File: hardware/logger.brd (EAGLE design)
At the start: 33.5 x 32.9 mm, 40 parts, among them J1 MICRO_USB_B_HIROSE_ZX62-B-5PA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, SW1 TVAF06-A020B-R, U2 NJM12888F, X1 FA-238

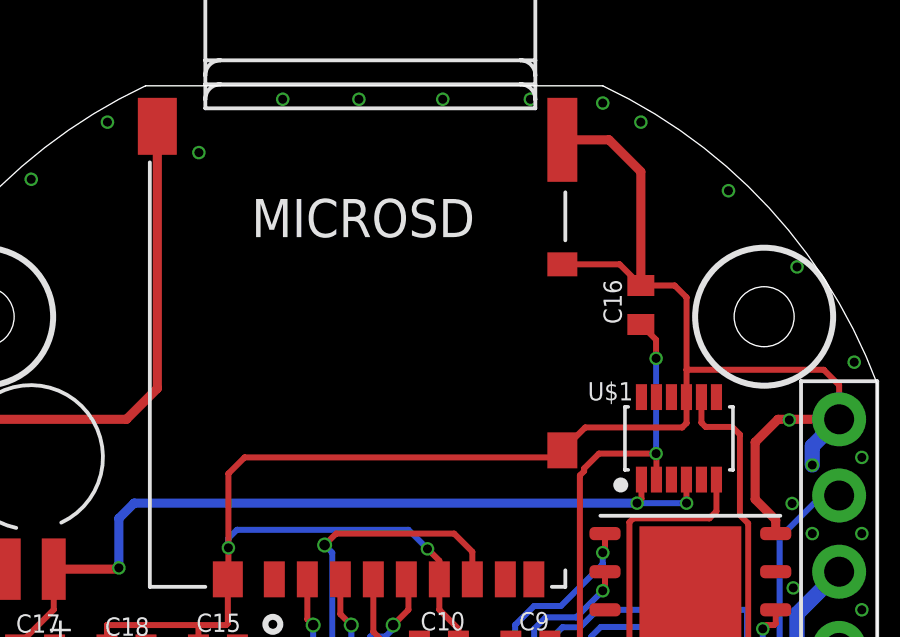
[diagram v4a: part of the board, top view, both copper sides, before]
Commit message: シルクを調整
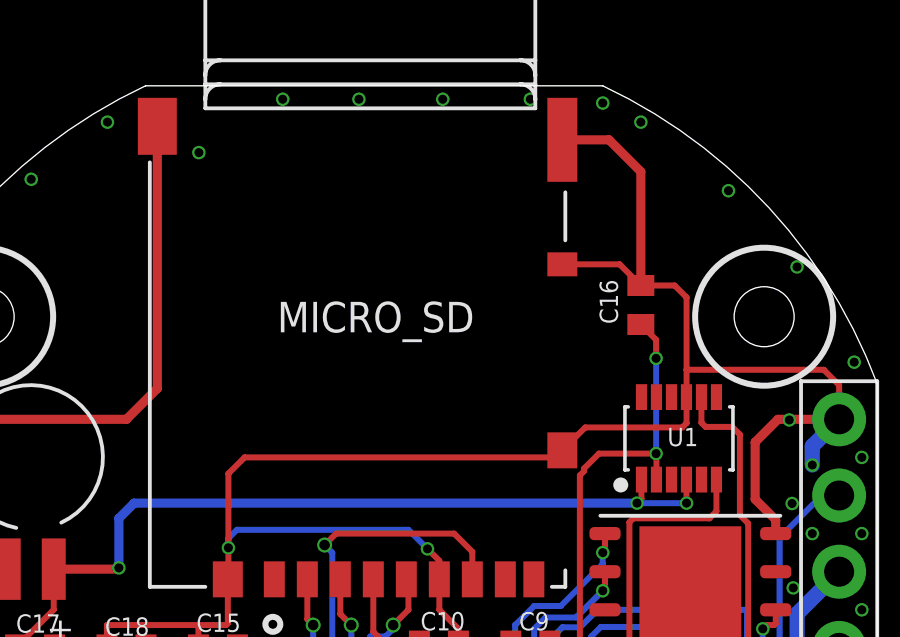
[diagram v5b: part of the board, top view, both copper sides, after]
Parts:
- renumbered BT1 to BAT, MICROSD to MICRO_SD, U$1 to U1
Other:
- board text added: "TERES Logger Module"
- board text removed: "TERES Module"
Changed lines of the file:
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@@
 <layer number="27" name="tValues" color="7" fill="1" visible="yes" active="yes"/>
 <layer number="28" name="bValues" color="7" fill="1" visible="yes" active="yes"/>
-<layer number="29" name="tStop" color="7" fill="3" visible="no" active="yes"/>
-<layer number="30" name="bStop" color="7" fill="6" visible="no" active="yes"/>
+<layer number="29" name="tStop" color="7" fill="3" visible="yes" active="yes"/>
+<layer number="30" name="bStop" color="7" fill="6" visible="yes" active="yes"/>
 <layer number="31" name="tCream" color="7" fill="4" visible="no" active="yes"/>
 <layer number="32" name="bCream" color="7" fill="5" visible="no" active="yes"/>
@@
 <wire x1="-6.349996875" y1="-16.735815625" x2="-16.764" y2="-6.275209375" width="0" layer="20" curve="-48.699765"/>
 <wire x1="16.764" y1="-6.2752125" x2="6.35" y2="-16.7358125" width="0" layer="20" curve="-48.699745"/>
-<text x="0" y="14.859" size="1.27" layer="29" font="vector" ratio="10" align="center">2022 WASA Rocket</text>
-<text x="0" y="14.859" size="1.27" layer="30" font="vector" ratio="10" rot="MR0" align="center">TERES Module</text>
+<text x="0" y="14.605" size="1.27" layer="30" font="vector" ratio="10" rot="MR0" align="center">2022 WASA Rocket</text>
+<text x="0" y="12.065" size="1.016" layer="30" font="vector" ratio="10" rot="MR0" align="center">TERES Logger Module</text>
 <circle x="13" y="-8.5" radius="2.3" width="0.2" layer="22"/>
 <circle x="-13" y="-8.5" radius="2.3" width="0.2" layer="22"/>
@@
 <element name="BOTTOM" library="pins" package="P5_2.54" value="P5_2.54" x="15.5" y="0" smashed="yes"/>
 <element name="U$2" library="pins" package="P2_2.54" value="P2_2_2.54" x="-11.43" y="-5.08" smashed="yes" rot="R90"/>
-<element name="MICROSD" library="dm3at-sf-pejm5" package="HRS_DM3AT-SF-PEJM5" value="DM3AT-SF-PEJM5" x="-0.127" y="-0.254" smashed="yes" rot="R180">
+<element name="MICRO_SD" library="dm3at-sf-pejm5" package="HRS_DM3AT-SF-PEJM5" value="DM3AT-SF-PEJM5" x="-0.127" y="-0.254" smashed="yes" rot="R180">
 <attribute name="DESCRIPTION" value=" DM3 RA SMT microSD memory card push/push " x="-0.127" y="-0.254" size="1.778" layer="27" rot="R180" display="off"/>
 <attribute name="DIGI-KEY_PART_NUMBER" value="HR1964CT-ND" x="-0.127" y="-0.254" size="1.778" layer="27" rot="R180" display="off"/>
@@
 <attribute name="MF" value="Hirose" x="-0.127" y="-0.254" size="1.778" layer="27" rot="R180" display="off"/>
 <attribute name="MP" value="DM3AT-SF-PEJM5" x="-0.127" y="-0.254" size="1.778" layer="27" rot="R180" display="off"/>
-<attribute name="NAME" x="3.35661875" y="12.42395" size="1.271940625" layer="25" rot="R180"/>
+<attribute name="NAME" x="0.05461875" y="8.48695" size="1.016" layer="25" font="vector" rot="R180" align="center"/>
 <attribute name="PACKAGE" value="None" x="-0.127" y="-0.254" size="1.778" layer="27" rot="R180" display="off"/>
 </element>
@@
 </element>
 <element name="C16" library="rcl" library_urn="urn:adsk.eagle:library:334" package="C0402" package3d_urn="urn:adsk.eagle:package:23626/2" value="" x="8.89" y="8.89" smashed="yes" rot="R90">
-<attribute name="NAME" x="8.255" y="8.255" size="0.6096" layer="25" font="vector" rot="R90"/>
+<attribute name="NAME" x="8.128" y="8.255" size="0.6096" layer="25" font="vector" rot="R90"/>
 <attribute name="POPULARITY" value="18" x="-1.27" y="0" size="1.778" layer="27" rot="R90" display="off"/>
 <attribute name="SPICEPREFIX" value="C" x="-1.27" y="0" size="1.778" layer="27" rot="R90" display="off"/>
 <attribute name="VALUE" x="10.795" y="8.255" size="1.27" layer="27" rot="R90"/>
 </element>
-<element name="BT1" library="MS414GE-FL26E" package="BAT_MS414GE-FL26E" value="MS414GE-FL26E" x="-11.43" y="3.81" smashed="yes" rot="R270">
+<element name="BAT" library="MS414GE-FL26E" package="BAT_MS414GE-FL26E" value="MS414GE-FL26E" x="-11.43" y="3.81" smashed="yes" rot="R270">
 <attribute name="AVAILABILITY" value="In Stock" x="-11.43" y="3.81" size="1.778" layer="27" rot="R270" display="off"/>
 <attribute name="DESCRIPTION" value=" Coin, 4.8mm 3 V Lithium Battery Rechargeable (Secondary) 2mAh " x="-11.43" y="3.81" size="1.778" layer="27" rot="R270" display="off"/>
 <attribute name="MF" value="Seiko" x="-11.43" y="3.81" size="1.778" layer="27" rot="R270" display="off"/>
 <attribute name="MP" value="MS414GE-FL26E" x="-11.43" y="3.81" size="1.778" layer="27" rot="R270" display="off"/>
-<attribute name="NAME" x="-7.493" y="7.747" size="1.27" layer="26" rot="R180"/>
+<attribute name="NAME" x="-11.43" y="3.81" size="1.016" layer="26" font="vector" rot="R180" align="center"/>
 <attribute name="PACKAGE" value="Custom Package Seiko" x="-11.43" y="3.81" size="1.778" layer="27" rot="R270" display="off"/>
 <attribute name="PRICE" value="None" x="-11.43" y="3.81" size="1.778" layer="27" rot="R270" display="off"/>
 <attribute name="PURCHASE-URL" value="https://pricing.snapeda.com/search/part/MS414GE-FL26E/?ref=eda" x="-11.43" y="3.81" size="1.778" layer="27" rot="R270" display="off"/>
 </element>
-<element name="U$1" library="rtc" package="VSOJ12" package3d_urn="urn:adsk.eagle:package:37886091/1" value="RX-8035LC" x="10.16" y="4.445" smashed="yes" rot="R90">
-<attribute name="NAME" x="7.874" y="6.3191" size="0.6096" layer="25" font="vector" rot="R180" align="bottom-center"/>
+<element name="U1" library="rtc" package="VSOJ12" package3d_urn="urn:adsk.eagle:package:37886091/1" value="RX-8035LC" x="10.16" y="4.445" smashed="yes" rot="R90">
+<attribute name="NAME" x="10.287" y="4.7951" size="0.6096" layer="25" font="vector" rot="R180" align="bottom-center"/>
 </element>
 <element name="C17" library="rcl" library_urn="urn:adsk.eagle:library:334" package="C0402" package3d_urn="urn:adsk.eagle:package:23626/2" value="0.1µF" x="-11.303" y="-2.54" smashed="yes">
@@
 <via x="7.366" y="-4.953" extent="1-16" drill="0.3"/>
 <wire x1="7.366" y1="-4.953" x2="3.239" y2="-4.953" width="0.2" layer="16"/>
-<contactref element="MICROSD" pad="4"/>
+<contactref element="MICRO_SD" pad="4"/>
 <contactref element="C15" pad="1"/>
 <contactref element="FLASH_LOG" pad="8"/>
 <contactref element="C16" pad="1"/>
-<contactref element="U$1" pad="2"/>
+<contactref element="U1" pad="2"/>
 <contactref element="C18" pad="1"/>
 <wire x1="-7.605" y1="-2.54" x2="-7.605" y2="-3.713" width="0.2" layer="1"/>
@@
 <via x="-11.4345" y="-4.6935" extent="1-16" drill="0.3"/>
 <via x="-11.592" y="-5.985" extent="1-16" drill="0.3"/>
-<contactref element="MICROSD" pad="SWA"/>
-<contactref element="MICROSD" pad="6"/>
+<contactref element="MICRO_SD" pad="SWA"/>
+<contactref element="MICRO_SD" pad="6"/>
 <contactref element="C15" pad="2"/>
-<contactref element="MICROSD" pad="P1"/>
-<contactref element="MICROSD" pad="P2"/>
-<contactref element="MICROSD" pad="P4"/>
-<contactref element="MICROSD" pad="P3"/>
+<contactref element="MICRO_SD" pad="P1"/>
+<contactref element="MICRO_SD" pad="P2"/>
+<contactref element="MICRO_SD" pad="P4"/>
+<contactref element="MICRO_SD" pad="P3"/>
 <contactref element="FLASH_LOG" pad="4"/>
 <contactref element="FLASH_LOG" pad="9"/>
 <contactref element="C16" pad="2"/>
-<contactref element="U$1" pad="9"/>
-<contactref element="BT1" pad="-"/>
+<contactref element="U1" pad="9"/>
+<contactref element="BAT" pad="-"/>
 <contactref element="C17" pad="2"/>
 <contactref element="C18" pad="2"/>
@@
 <signal name="SPI0_MISO">
 <contactref element="RP1" pad="31"/>
-<contactref element="MICROSD" pad="7"/>
+<contactref element="MICRO_SD" pad="7"/>
 <wire x1="-1.27" y1="-7.09" x2="-0.26" y2="-7.09" width="0.2" layer="1"/>
 <via x="-1.397" y="-3.81" extent="1-16" drill="0.35"/>
@@
 <signal name="SPI0_CS">
 <contactref element="RP1" pad="32"/>
-<contactref element="MICROSD" pad="2"/>
+<contactref element="MICRO_SD" pad="2"/>
 <wire x1="-0.26" y1="-7.49" x2="-1.527" y2="-7.49" width="0.2" layer="1"/>
 <wire x1="-1.651" y1="-7.366" x2="-1.527" y2="-7.49" width="0.2" layer="1"/>
@@
 <signal name="SPI0_SCK">
 <contactref element="RP1" pad="29"/>
-<contactref element="MICROSD" pad="5"/>
+<contactref element="MICRO_SD" pad="5"/>
 <wire x1="-0.26" y1="-6.29" x2="-0.26" y2="-6.078925" width="0.2" layer="1"/>
 <wire x1="-0.26" y1="-6.078925" x2="-0.3322" y2="-6.006725" width="0.2" layer="1"/>
@@
 <signal name="SPI0_MOSI">
 <contactref element="RP1" pad="30"/>
-<contactref element="MICROSD" pad="3"/>
+<contactref element="MICRO_SD" pad="3"/>
 <wire x1="-0.26" y1="-6.69" x2="-0.333" y2="-6.617" width="0.2" layer="1"/>
 <wire x1="-0.333" y1="-6.617" x2="-0.75938125" y2="-6.617" width="0.2" layer="1"/>
@@
 <signal name="I2C0_SDA">
 <contactref element="RP1" pad="11"/>
-<contactref element="U$1" pad="8"/>
+<contactref element="U1" pad="8"/>
 <wire x1="10.91" y1="5.82" x2="10.91" y2="4.965" width="0.2" layer="1"/>
 <wire x1="10.91" y1="4.965" x2="11.049" y2="4.826" width="0.2" layer="1"/>
@@
 <signal name="I2C0_SCL">
 <contactref element="RP1" pad="12"/>
-<contactref element="U$1" pad="6"/>
+<contactref element="U1" pad="6"/>
 <wire x1="11.41" y1="3.07" x2="11.41" y2="2.012" width="0.2" layer="1"/>
 <wire x1="11.41" y1="2.012" x2="11.176" y2="1.778" width="0.2" layer="1"/>
@@
 </signal>
 <signal name="SD">
-<contactref element="MICROSD" pad="SWB"/>
+<contactref element="MICRO_SD" pad="SWB"/>
 </signal>
 <signal name="N$1">
-<contactref element="BT1" pad="+"/>
-<contactref element="U$1" pad="4"/>
-<contactref element="U$1" pad="1"/>
+<contactref element="BAT" pad="+"/>
+<contactref element="U1" pad="4"/>
+<contactref element="U1" pad="1"/>
 <contactref element="C17" pad="1"/>
 <wire x1="-10.68" y1="0.085" x2="-10.68" y2="-1.267" width="0.2" layer="1"/>

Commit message: 若干修正
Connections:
- removed net PWM5_B: RP1.14
- net SD: now also RP1.14
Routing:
- net SD: track 0.00 -> 9.47 mm, vias 0 -> 2
- net VDD: track 100.0 -> 100.7 mm
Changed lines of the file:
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@@
 <wire x1="2.975" y1="-12.325" x2="2.975" y2="-13.06155" width="0.2" layer="1"/>
 <via x="7.366" y="-4.953" extent="1-16" drill="0.3"/>
-<wire x1="7.366" y1="-4.953" x2="3.239" y2="-4.953" width="0.2" layer="16"/>
+<wire x1="7.366" y1="-4.953" x2="6.604" y2="-5.715" width="0.2" layer="16"/>
+<wire x1="6.604" y1="-5.715" x2="4.001" y2="-5.715" width="0.2" layer="16"/>
 <contactref element="MICRO_SD" pad="4"/>
 <contactref element="C15" pad="1"/>
@@
 <wire x1="2.54" y1="-4.381" x2="2.667" y2="-4.381" width="0.2" layer="16"/>
 <wire x1="0.508" y1="-2.667" x2="2.222" y2="-4.381" width="0.2" layer="16"/>
-<wire x1="2.667" y1="-4.381" x2="3.239" y2="-4.953" width="0.2" layer="16"/>
+<wire x1="2.667" y1="-4.381" x2="4.001" y2="-5.715" width="0.2" layer="16"/>
 <wire x1="1.509" y1="-2.413" x2="1.382" y2="-2.54" width="0.2" layer="1"/>
 <wire x1="9.398" y1="7.112" x2="9.398" y2="3.937" width="0.2" layer="16"/>
@@
 <via x="11.811" y="-9.652" extent="1-16" drill="0.3"/>
 <via x="3.683" y="-2.413" extent="1-16" drill="0.3"/>
-<via x="3.937" y="-3.81" extent="1-16" drill="0.3"/>
+<via x="3.937" y="-4.572" extent="1-16" drill="0.3"/>
 <via x="-11.049" y="-13.462" extent="1-16" drill="0.3"/>
 <via x="-8.124" y="-8.0145" extent="1-16" drill="0.3"/>
@@
 <wire x1="4.557" y1="-2.413" x2="3.683" y2="-2.413" width="0.2" layer="1"/>
 <wire x1="3.683" y1="-2.413" x2="3.556" y2="-2.54" width="0.2" layer="16"/>
-<wire x1="3.556" y1="-2.54" x2="3.556" y2="-3.81" width="0.2" layer="16"/>
-<wire x1="3.556" y1="-3.81" x2="3.937" y2="-3.81" width="0.2" layer="16"/>
-<wire x1="3.937" y1="-3.81" x2="4.175" y2="-4.048" width="0.2" layer="1"/>
-<wire x1="4.175" y1="-4.048" x2="4.175" y2="-5.455" width="0.2" layer="1"/>
+<wire x1="3.556" y1="-2.54" x2="3.556" y2="-4.572" width="0.2" layer="16"/>
+<wire x1="3.556" y1="-4.572" x2="3.937" y2="-4.572" width="0.2" layer="16"/>
+<wire x1="3.937" y1="-4.572" x2="4.175" y2="-4.81" width="0.2" layer="1"/>
+<wire x1="4.175" y1="-4.81" x2="4.175" y2="-5.455" width="0.2" layer="1"/>
 <wire x1="10.541" y1="-0.635" x2="10.541" y2="-5.476" width="0.2" layer="1"/>
 <wire x1="10.541" y1="-5.476" x2="9.667" y2="-6.35" width="0.2" layer="1"/>
@@
 <signal name="PWM5_A">
 <contactref element="RP1" pad="13"/>
-</signal>
-<signal name="PWM5_B">
-<contactref element="RP1" pad="14"/>
 </signal>
 <signal name="SW">
@@
 <signal name="SD">
 <contactref element="MICRO_SD" pad="SWB"/>
+<contactref element="RP1" pad="14"/>
+<wire x1="6.61" y1="-6.29" x2="7.172" y2="-6.29" width="0.1524" layer="1"/>
+<wire x1="7.172" y1="-6.29" x2="7.366" y2="-6.096" width="0.1524" layer="1"/>
+<wire x1="7.366" y1="-6.096" x2="7.366" y2="-5.8225" width="0.1524" layer="1"/>
+<wire x1="7.366" y1="-5.8225" x2="6.5835" y2="-5.04" width="0.1524" layer="1"/>
+<via x="6.5835" y="-5.04" extent="1-16" drill="0.3"/>
+<wire x1="6.5835" y1="-5.04" x2="5.9885" y2="-4.445" width="0.1524" layer="16"/>
+<wire x1="5.9885" y1="-4.445" x2="4.572" y2="-4.445" width="0.1524" layer="16"/>
+<wire x1="4.572" y1="-4.445" x2="4.191" y2="-4.064" width="0.1524" layer="16"/>
+<wire x1="4.191" y1="-4.064" x2="4.191" y2="-1.524" width="0.1524" layer="16"/>
+<via x="4.191" y="-1.524" extent="1-16" drill="0.3"/>
+<wire x1="4.191" y1="-1.524" x2="4.5308" y2="-1.1842" width="0.1524" layer="1"/>
+<wire x1="4.5308" y1="-1.1842" x2="4.83766875" y2="-1.1842" width="0.1524" layer="1"/>
+<wire x1="4.83766875" y1="-1.1842" x2="5.323" y2="-0.69886875" width="0.1524" layer="1"/>
+<wire x1="5.323" y1="-0.69886875" x2="5.323" y2="-0.254" width="0.1524" layer="1"/>
 </signal>
 <signal name="N$1">
